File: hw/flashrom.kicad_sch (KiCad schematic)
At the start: 12 parts, among them J1 Conn_01x03_Male, J3 Conn_01x03_Male, U1 Kickstart_Socket_A4000, U2 29F800

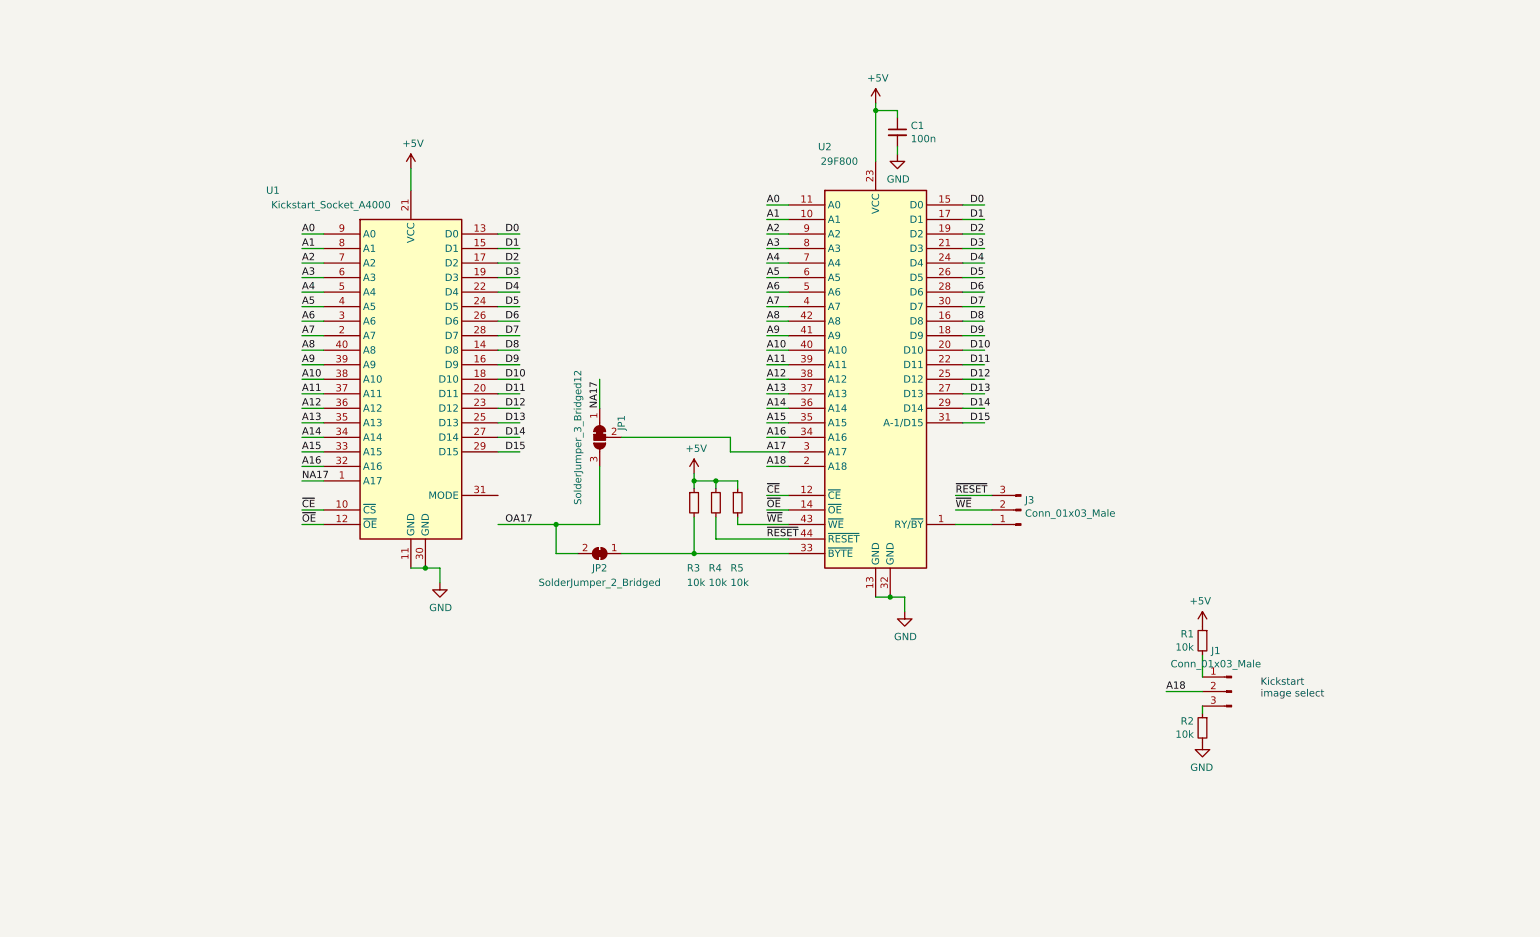
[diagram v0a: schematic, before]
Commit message: switch flash to tsop, add tvs, and route pcb
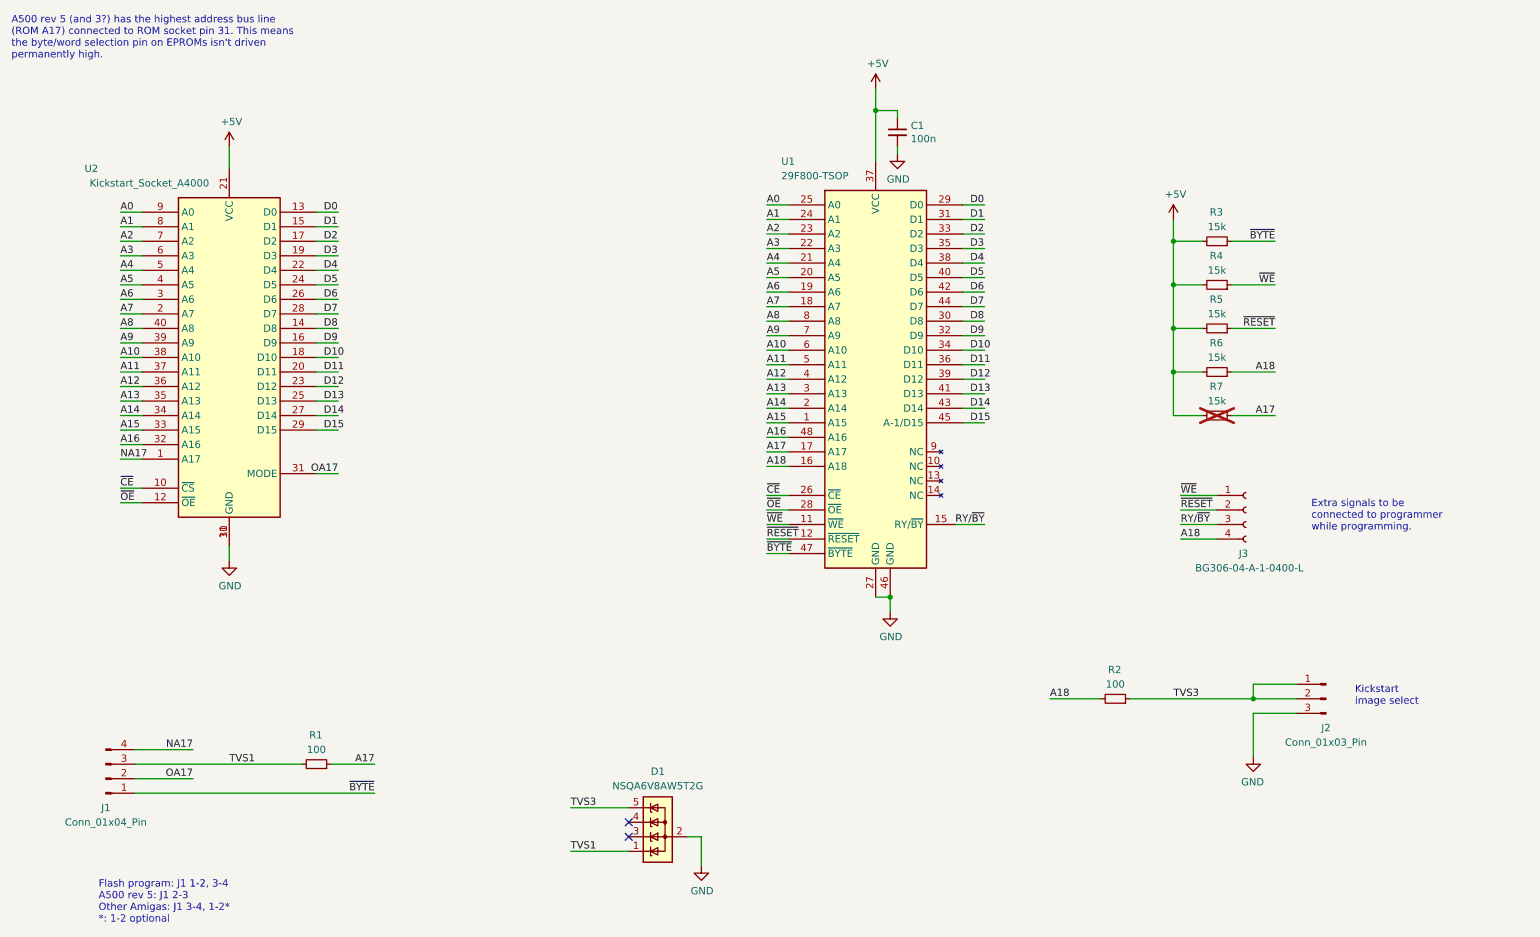
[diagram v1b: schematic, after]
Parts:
- removed J3: Conn_01x03_Male, Connector_PinHeader_2.54mm:PinHeader_1x03_P2.54mm_Horizontal, symbol Connector:Conn_01x03_Pin
- removed JP1: SolderJumper_3_Bridged12, Jumper:SolderJumper-3_P1.3mm_Open_RoundedPad1.0x1.5mm, symbol Jumper:SolderJumper_3_Bridged12
- removed JP2: SolderJumper_2_Bridged, Jumper:SolderJumper-2_P1.3mm_Open_RoundedPad1.0x1.5mm, symbol Jumper:SolderJumper_2_Bridged
- removed R2: 10k, Resistor_SMD:R_0805_2012Metric, symbol Device:R_Small
- removed U2: 29F800, Package_SO:PSOP-44_16.9x27.17mm_P1.27mm, symbol Memory_Flash_29F800:29F800
- added D1: NSQA6V8AW5T2G, Package_TO_SOT_SMD:SOT-353_SC-70-5, symbol Power_Protection:SP0504BAJT
- added J1: Conn_01x04_Pin, Connector_PinHeader_2.54mm:PinHeader_1x04_P2.54mm_Horizontal, symbol Connector:Conn_01x04_Pin
- added J3: BG306-04-A-1-0400-L, Connector_PinSocket_2.54mm:PinSocket_1x04_P2.54mm_Vertical_SMD_Pin1Left, symbol Connector:Conn_01x04_Socket
- added R1: 100, Resistor_SMD:R_0603_1608Metric, symbol Device:R_Small
- added R6, R7: 15k, Resistor_SMD:R_0603_1608Metric, symbol Device:R_Small
- added U1: 29F800-TSOP, Package_SO:TSOP-I-48_18.4x12mm_P0.5mm, symbol Memory_Flash_29F800:29F800-TSOP
- C1: footprint Capacitor_SMD:C_0805_2012Metric_Pad1.15x1.40mm_HandSolder -> Capacitor_SMD:C_0603_1608Metric
- J2: renamed from J1; value Conn_01x03_Male -> Conn_01x03_Pin; footprint Connector_PinHeader_2.54mm:PinHeader_1x03_P2.54mm_Vertical -> Connector_PinHeader_2.54mm:PinHeader_1x03_P2.54mm_Horizontal
- R2: renamed from R1; value 10k -> 100; footprint Resistor_SMD:R_0805_2012Metric -> Resistor_SMD:R_0603_1608Metric
- R3, R4, R5: value 10k -> 15k; footprint Resistor_SMD:R_0805_2012Metric -> Resistor_SMD:R_0603_1608Metric
- renumbered U1 to U2
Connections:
- net +5V: now also R3.2, R4.2, R5.2, R6.2, R7.2, U1.37 (VCC); no longer R2.1, R3.1, R4.1, R5.1
- net A0: now also U1.25 (A0)
- net A1: now also U1.24 (A1)
- net A10: now also U1.6 (A10)
- net A11: now also U1.5 (A11)
- net A12: now also U1.4 (A12)
- net A13: now also U1.3 (A13)
- net A14: now also U1.2 (A14)
- net A15: now also U1.1 (A15)
- net A16: now also U1.48 (A16)
- net A17: now also R1.1, R7.1, U1.17 (A17)
- net A18: now also R2.2, J3.4 (Pin_4), R6.1, U1.16 (A18); no longer J2.2 (Pin_2)
- net A2: now also U1.23 (A2)
- net A3: now also U1.22 (A3)
- net A4: now also U1.21 (A4)
- net A5: now also U1.20 (A5)
- net A6: now also U1.19 (A6)
- net A7: now also U1.18 (A7)
- net A8: now also U1.8 (A8)
- net A9: now also U1.7 (A9)
- net D0: now also U1.29 (D0)
- net D1: now also U1.31 (D1)
- net D10: now also U1.34 (D10)
- net D11: now also U1.36 (D11)
- net D12: now also U1.39 (D12)
- net D13: now also U1.41 (D13)
- net D14: now also U1.43 (D14)
- net D15: now also U1.45 (A-1/D15)
- net D2: now also U1.33 (D2)
- net D3: now also U1.35 (D3)
- net D4: now also U1.38 (D4)
- net D5: now also U1.40 (D5)
- net D6: now also U1.42 (D6)
- net D7: now also U1.44 (D7)
- net D8: now also U1.30 (D8)
- net D9: now also U1.32 (D9)
- net GND: now also J2.3 (Pin_3), D1.2 (A), U1.27 (GND), U1.46 (GND)
- net NA17: now also J1.4 (Pin_4)
- net OA17: now also U2.31 (MODE), J1.2 (Pin_2)
- net ~{CE}: now also U1.26 (~{CE})
- net ~{OE}: now also U1.28 (~{OE})
- net ~{RESET}: now also R5.1, J3.2 (Pin_2), U1.12 (~{RESET}); no longer R4.2
- net ~{WE}: now also R4.1, J3.1 (Pin_1), U1.11 (~{WE}); no longer R5.2
- net TVS3: now reaches J2.1 (Pin_1)
- net TVS3: now also J2.2 (Pin_2), R2.1, D1.5 (K); no longer R2.2
- new net RY/~{BY}: J3.3 (Pin_3), U1.15 (RY/~{BY})
- new net TVS1: D1.1 (K), J1.3 (Pin_3), R1.2
- new net ~{BYTE}: J1.1 (Pin_1), R3.1, U1.47 (~{BYTE})
- no-connect marks 0 -> 2
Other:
- note added: "A500 rev 5 (and 3?) has the highest address bus line (ROM A17) connected to ROM socket pin 31. This means the byte/word selection pin on EPROMs isn't driven permanently high."
- note added: "Extra signals to be connected to programmer while programming."
- note added: "Flash program: J1 1-2, 3-4 A500 rev 5: J1 2-3 Other Amigas: J1 3-4, 1-2* *: 1-2 optional"
- moved on the sheet: J2, R2

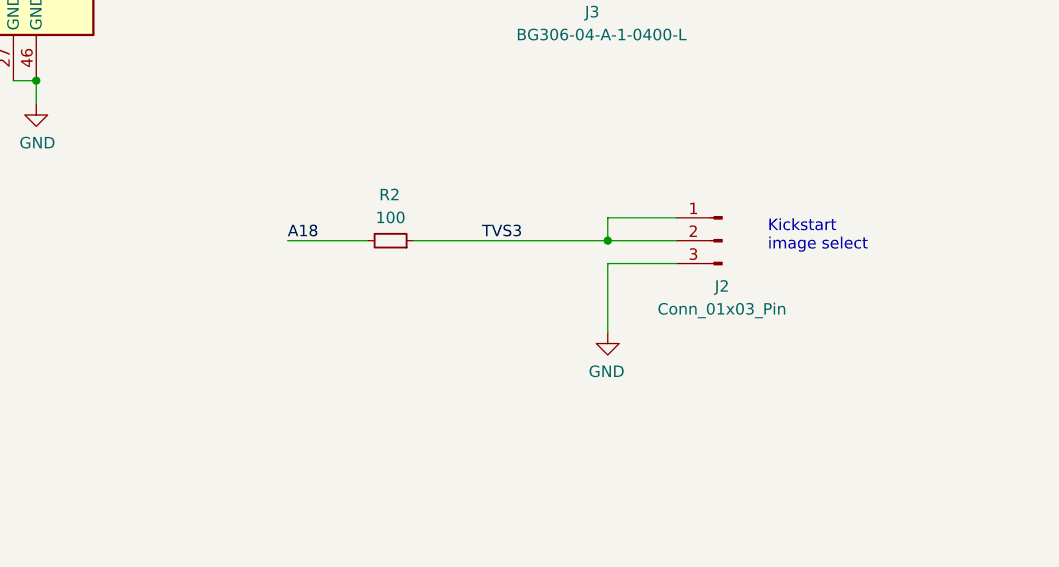
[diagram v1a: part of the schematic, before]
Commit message: change pin 1 of j2 to /WE to support a wire for in-system programming
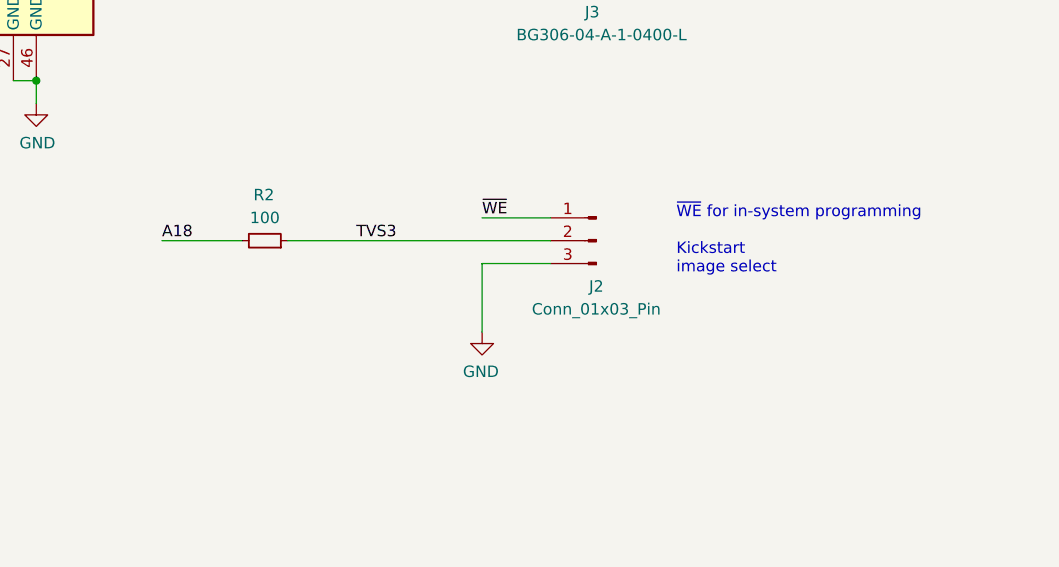
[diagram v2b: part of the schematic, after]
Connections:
- net TVS3: no longer J2.1 (Pin_1)
- net ~{WE}: now also J2.1 (Pin_1)
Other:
- note added: "~{WE} for in-system programming Kickstart image select"
- note removed: "Kickstart image select"
- moved on the sheet: J2, R2

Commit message: switch j3 footprint to horizontal pin header
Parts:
- J3: value BG306-04-A-1-0400-L -> Conn_01x04_Pin; footprint Connector_PinSocket_2.54mm:PinSocket_1x04_P2.54mm_Vertical_SMD_Pin1Left -> Connector_Harwin:Harwin_M20-89004xx_1x04_P2.54mm_Horizontal; symbol Connector:Conn_01x04_Socket -> Connector:Conn_01x04_Pin
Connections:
- net A18: now also J3.1 (Pin_1); no longer J3.4 (Pin_4)
- net RY/~{BY}: now also J3.2 (Pin_2); no longer J3.3 (Pin_3)
- net ~{RESET}: now also J3.3 (Pin_3); no longer J3.2 (Pin_2)
- net ~{WE}: now also J3.4 (Pin_4); no longer J3.1 (Pin_1)
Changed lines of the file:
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@@
     (stroke (width 0) (type default))
   )
-  (wire (pts (xy 232.41 106.68) (xy 226.06 106.68))
+  (wire (pts (xy 232.41 114.3) (xy 226.06 114.3))
     (stroke (width 0) (type default))
   )
@@
     (stroke (width 0) (type default))
   )
-  (wire (pts (xy 226.06 114.3) (xy 232.41 114.3))
+  (wire (pts (xy 226.06 106.68) (xy 232.41 106.68))
     (stroke (width 0) (type default))
   )
@@
     (stroke (width 0) (type default))
   )
+  (wire (pts (xy 226.06 111.76) (xy 232.41 111.76))
+    (stroke (width 0) (type default))
+  )
   (wire (pts (xy 226.06 109.22) (xy 232.41 109.22))
-    (stroke (width 0) (type default))
-  )
-  (wire (pts (xy 226.06 111.76) (xy 232.41 111.76))
     (stroke (width 0) (type default))
   )
@@
     (effects (font (size 1.27 1.27)) (justify left bottom))
   )
-  (label "A18" (at 226.06 114.3 0) (fields_autoplaced)
+  (label "A18" (at 226.06 106.68 0) (fields_autoplaced)
     (effects (font (size 1.27 1.27)) (justify left bottom))
   )
@@
     (effects (font (size 1.27 1.27)) (justify left bottom))
   )
-  (label "~{RESET}" (at 226.06 109.22 0) (fields_autoplaced)
+  (label "~{RESET}" (at 226.06 111.76 0) (fields_autoplaced)
     (effects (font (size 1.27 1.27)) (justify left bottom))
   )
@@
     (effects (font (size 1.27 1.27)) (justify left bottom))
   )
-  (label "~{WE}" (at 226.06 106.68 0) (fields_autoplaced)
+  (label "~{WE}" (at 226.06 114.3 0) (fields_autoplaced)
     (effects (font (size 1.27 1.27)) (justify left bottom))
   )
@@
     (effects (font (size 1.27 1.27)) (justify left bottom))
   )
-  (label "RY{slash}~{BY}" (at 226.06 111.76 0) (fields_autoplaced)
+  (label "RY{slash}~{BY}" (at 226.06 109.22 0) (fields_autoplaced)
     (effects (font (size 1.27 1.27)) (justify left bottom))
   )
@@
     )
   )
-  (symbol (lib_id "Connector:Conn_01x04_Socket") (at 237.49 109.22 0) (unit 1)
-    (in_bom yes) (on_board yes) (dnp no)
-    (property "Reference" "J3" (at 236.22 116.84 0)
+  (symbol (lib_id "Connector:Conn_01x04_Pin") (at 237.49 109.22 0) (mirror y) (unit 1)
+    (in_bom yes) (on_board yes) (dnp no)
+    (property "Reference" "J3" (at 238.76 116.84 0)
       (effects (font (size 1.27 1.27)) (justify left))
     )
-    (property "Value" "BG306-04-A-1-0400-L" (at 228.6 119.38 0)
+    (property "Value" "Conn_01x04_Pin" (at 246.38 119.38 0)
       (effects (font (size 1.27 1.27)) (justify left))
     )
-    (property "Footprint" "Connector_PinSocket_2.54mm:PinSocket_1x04_P2.54mm_Vertical_SMD_Pin1Left" (at 237.49 109.22 0)
-      (effects (font (size 1.27 1.27)) hide)
-    )
-    (property "Datasheet" "https://www.mouser.dk/datasheet/2/837/BG306-1948788.pdf" (at 237.49 109.22 0)
-      (effects (font (size 1.27 1.27)) hide)
-    )
+    (property "Footprint" "Connector_Harwin:Harwin_M20-89004xx_1x04_P2.54mm_Horizontal" (at 237.49 109.22 0)
+      (effects (font (size 1.27 1.27)) hide)
+    )
+    (property "Datasheet" "~" (at 237.49 109.22 0)
+      (effects (font (size 1.27 1.27)) hide)
+    )

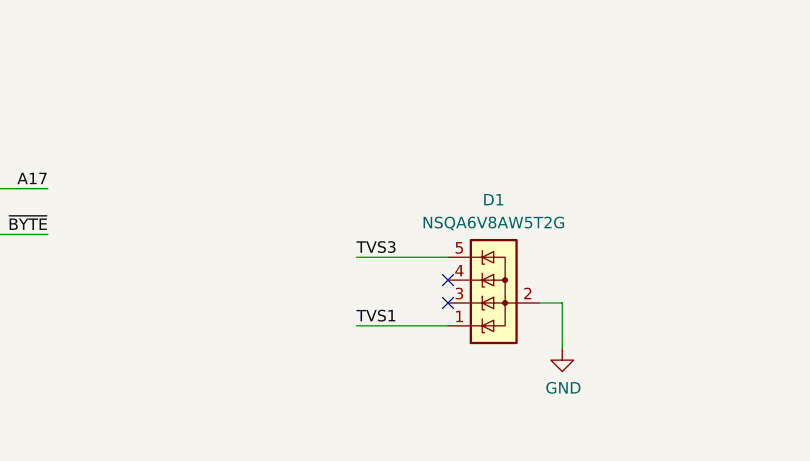
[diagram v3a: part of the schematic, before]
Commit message: switch j1 and j2 footprints to smd horizontal header
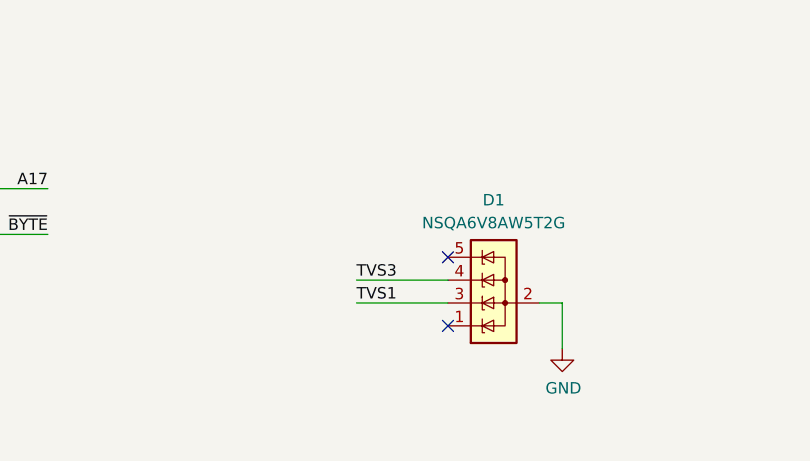
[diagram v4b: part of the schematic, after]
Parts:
- J1: footprint Connector_PinHeader_2.54mm:PinHeader_1x04_P2.54mm_Horizontal -> Connector_Harwin:Harwin_M20-89004xx_1x04_P2.54mm_Horizontal
- J2: footprint Connector_PinHeader_2.54mm:PinHeader_1x03_P2.54mm_Horizontal -> Connector_Harwin:Harwin_M20-89003xx_1x03_P2.54mm_Horizontal
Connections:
- net TVS1: now also D1.3 (K); no longer D1.1 (K)
- net TVS3: now also D1.4 (K); no longer D1.5 (K)
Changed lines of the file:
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@@
   (junction (at 224.79 69.85) (diameter 0) (color 0 0 0 0)
   )
-  (no_connect (at 129.54 163.83))
-  (no_connect (at 129.54 166.37))
+  (no_connect (at 129.54 161.29))
+  (no_connect (at 129.54 168.91))
   (wire (pts (xy 224.79 139.7) (xy 232.41 139.7))
     (stroke (width 0) (type default))
@@
     (stroke (width 0) (type default))
   )
-  (wire (pts (xy 119.38 168.91) (xy 129.54 168.91))
+  (wire (pts (xy 119.38 166.37) (xy 129.54 166.37))
     (stroke (width 0) (type default))
   )
@@
     (stroke (width 0) (type default))
   )
-  (wire (pts (xy 119.38 161.29) (xy 129.54 161.29))
+  (wire (pts (xy 119.38 163.83) (xy 129.54 163.83))
     (stroke (width 0) (type default))
   )
@@
     (effects (font (size 1.27 1.27)) (justify left bottom))
   )
-  (label "TVS3" (at 119.38 161.29 0) (fields_autoplaced)
+  (label "TVS3" (at 119.38 163.83 0) (fields_autoplaced)
     (effects (font (size 1.27 1.27)) (justify left bottom))
   )
@@
     (effects (font (size 1.27 1.27)) (justify left bottom))
   )
-  (label "TVS1" (at 119.38 168.91 0) (fields_autoplaced)
+  (label "TVS1" (at 119.38 166.37 0) (fields_autoplaced)
     (effects (font (size 1.27 1.27)) (justify left bottom))
   )
@@
       (effects (font (size 1.27 1.27)))
     )
-    (property "Footprint" "Connector_PinHeader_2.54mm:PinHeader_1x03_P2.54mm_Horizontal" (at 237.49 142.24 0)
+    (property "Footprint" "Connector_Harwin:Harwin_M20-89003xx_1x03_P2.54mm_Horizontal" (at 237.49 142.24 0)
       (effects (font (size 1.27 1.27)) hide)
     )
@@
       (effects (font (size 1.27 1.27)))
     )
-    (property "Footprint" "Connector_PinHeader_2.54mm:PinHeader_1x04_P2.54mm_Horizontal" (at 38.1 156.21 0)
-      (effects (font (size 1.27 1.27)) hide)
-    )
+    (property "Footprint" "Connector_Harwin:Harwin_M20-89004xx_1x04_P2.54mm_Horizontal" (at 38.1 156.21 0)
+      (effects (font (size 1.27 1.27)) hide)
+    )

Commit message: update text
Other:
- note added: "A500 rev 5 (and older?) has the highest address line (ROM A17) connected to ROM socket pin 31 instead of pin 1. This means the byte/word selection pin on EPROMs isn't driven permanently high."
- note removed: "A500 rev 5 (and 3?) has the highest address bus line (ROM A17) connected to ROM socket pin 31. This means the byte/word selection pin on EPROMs isn't driven permanently high."
- title: (none) -> 27C400 compatible programmable ROM
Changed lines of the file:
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@@
 (kicad_sch (version 20230121) (generator eeschema)
   (paper "A4")
+  (title_block
+    (title "27C400 compatible programmable ROM")
+    (comment 1 "By Jesper Matthiesen")
+  )
   (junction (at 224.79 62.23) (diameter 0) (color 0 0 0 0)
   )
@@
     (stroke (width 0) (type default))
   )
-  (text "A500 rev 5 (and 3?) has the highest address bus line\n(ROM A17) connected to ROM socket pin 31. This means\nthe byte/word selection pin on EPROMs isn't driven\npermanently high.\n"
+  (text "A500 rev 5 (and older?) has the highest address line\n(ROM A17) connected to ROM socket pin 31 instead of pin 1.\nThis means the byte/word selection pin on EPROMs isn't driven\npermanently high. \n"
     (at 21.59 30.48 0)
     (effects (font (size 1.27 1.27)) (justify left bottom))
